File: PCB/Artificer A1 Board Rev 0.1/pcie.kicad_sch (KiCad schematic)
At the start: 1 part, among them U7 X3113WVS-36-9TV01

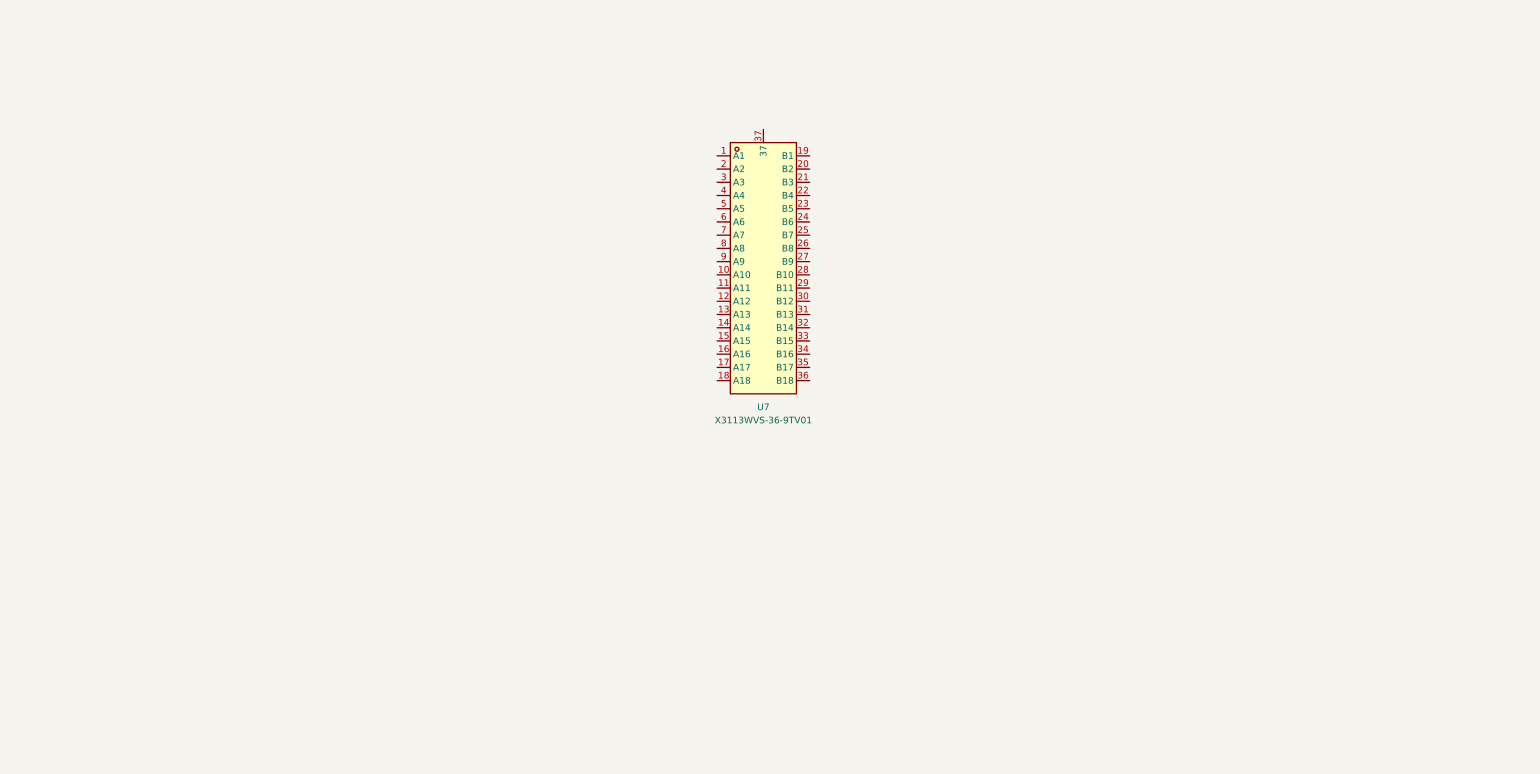
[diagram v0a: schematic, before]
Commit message: schematic update
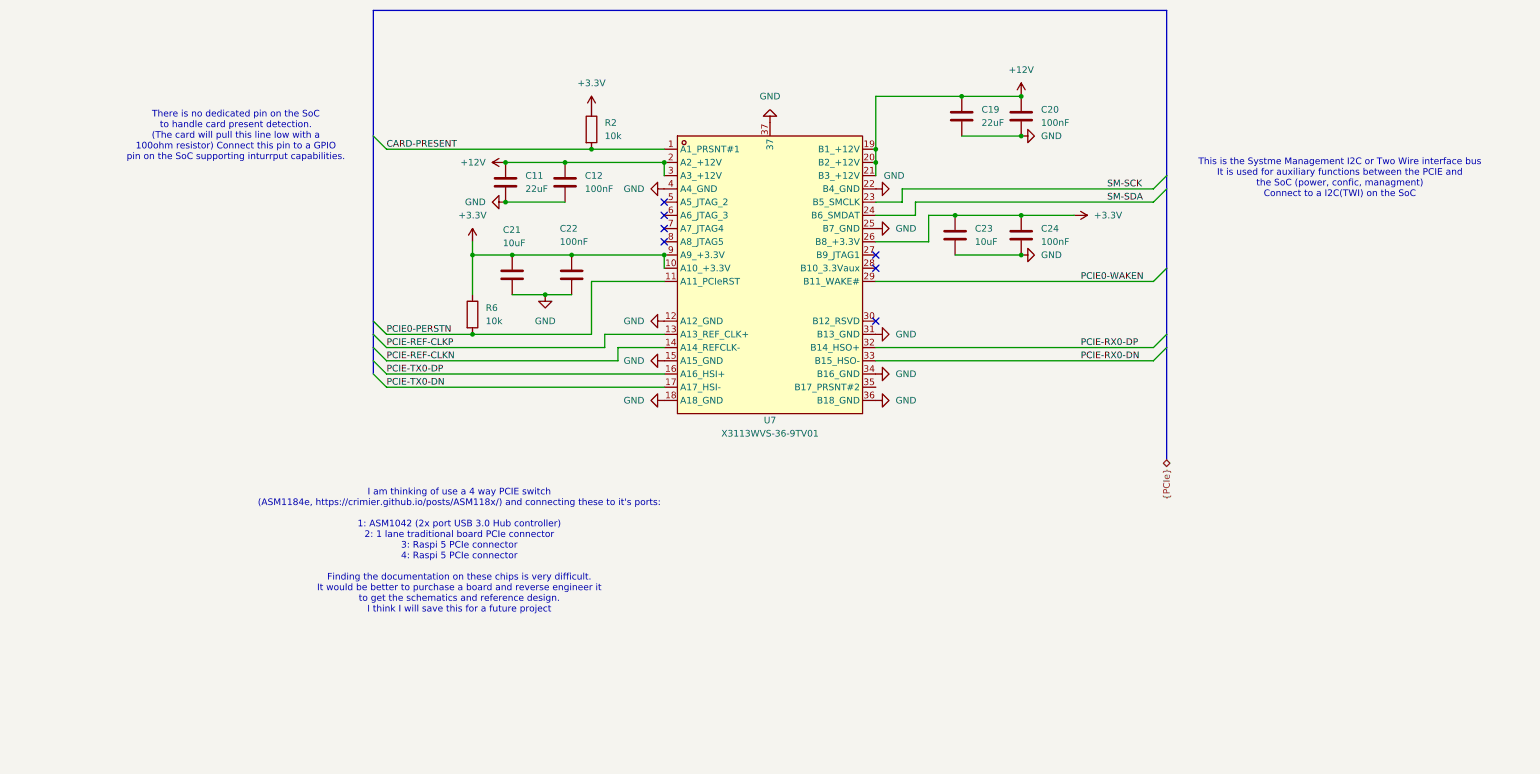
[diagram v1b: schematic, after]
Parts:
- added C11, C19: 22uF, symbol Device:C
- added C12, C20, C22, C24: 100nF, symbol Device:C
- added C21, C23: 10uF, symbol Device:C
- added R2, R6: 10k, symbol Device:R
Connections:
- net CARD-PRESENT: now reaches U7.1 (A1_PRSNT#1)
- net CARD-PRESENT: now also R2.2
- net +3.3V: now reaches U7.10 (A10_+3.3V)
- net +3.3V: now also U7.26 (B8_+3.3V), U7.9 (A9_+3.3V), C21.1, C22.1, C23.1, C24.1, R2.1, R6.1
- net PCIE0-PERSTN: now reaches U7.11 (A11_PCIeRST)
- net PCIE0-PERSTN: now also R6.2
- net GND: now reaches U7.12 (A12_GND)
- net GND: now also U7.15 (A15_GND), U7.18 (A18_GND), U7.22 (B4_GND), U7.25 (B7_GND), U7.31 (B13_GND), U7.34 (B16_GND), U7.36 (B18_GND), U7.37, U7.4 (A4_GND), C11.2, C12.2, C19.2, C20.2, C21.2, C22.2, C23.2, C24.2
- net PCIE-REF-CLKP : now reaches U7.13 (A13_REF_CLK+)
- net PCIE-REF-CLKN : now reaches U7.14 (A14_REFCLK-)
- net PCIE-TX0-DP: now reaches U7.16 (A16_HSI+)
- net PCIE-TX0-DN: now reaches U7.17 (A17_HSI-)
- net +12V: now reaches U7.19 (B1_+12V)
- net +12V: now also U7.2 (A2_+12V), U7.20 (B2_+12V), U7.21 (B3_+12V), U7.3 (A3_+12V), C11.1, C12.1, C19.1, C20.1
- net SM-SCK: now reaches U7.23 (B5_SMCLK)
- net SM-SDA: now reaches U7.24 (B6_SMDAT)
- net PCIE0-WAKEN : now reaches U7.29 (B11_WAKE#)
- net PCIE-RX0-DP: now reaches U7.32 (B14_HSO+)
- net PCIE-RX0-DN: now reaches U7.33 (B15_HSO-)
- no-connect marks 0 -> 7
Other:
- note added: "I am thinking of use a 4 way PCIE switch (ASM1184e, https://crimier.github.io/posts/ASM118x/) and connecting these to it's ports: 1: ASM1042 (2x port USB 3.0 Hub controller) 2: 1 lane traditional board PCIe connector 3: Raspi 5 PCIe connector 4: Raspi 5 PCIe connector Finding the documentation on these chips is very difficult. It would be better to purchase a board and reverse engineer it to get 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"
- note added: "There is no dedicated pin on the SoC to handle card present detection. (The card will pull this line low with a 100ohm resistor) Connect this pin to a GPIO pin on the SoC supporting inturrput capabilities."
- note added: "This is the Systme Management I2C or Two Wire interface bus It is used for auxiliary functions between the PCIE and the SoC (power, confic, managment) Connect to a I2C(TWI) on the SoC"
- moved on the sheet: U7

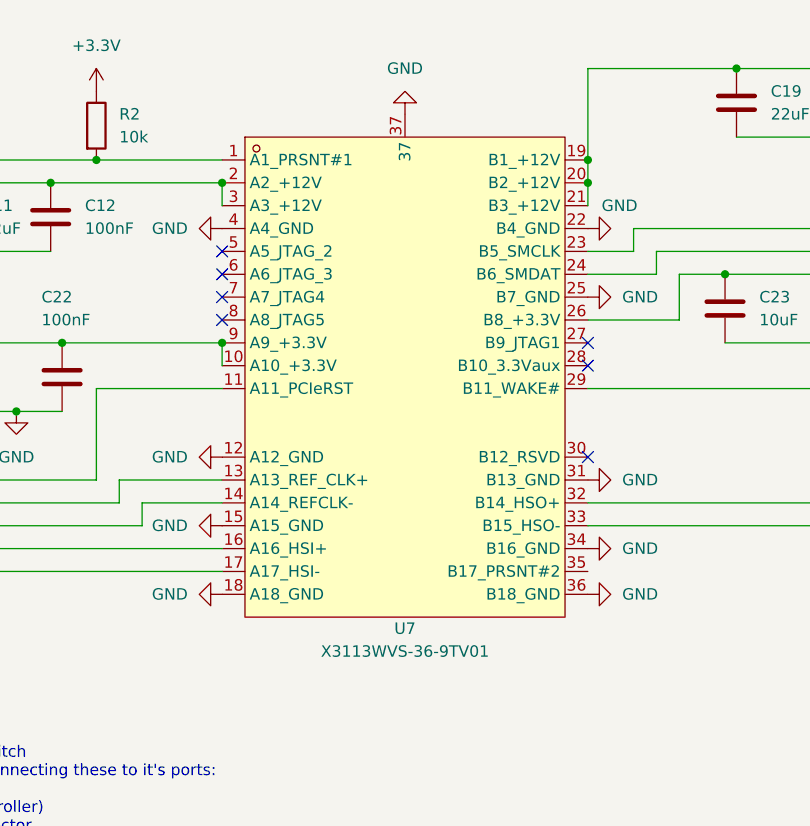
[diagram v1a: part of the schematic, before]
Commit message: localized libraries
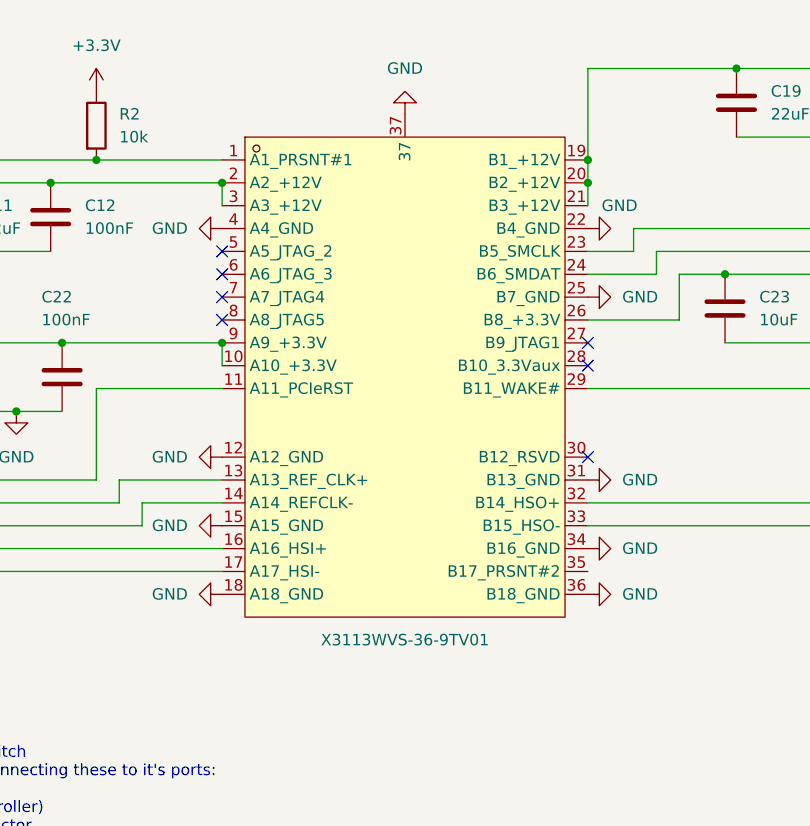
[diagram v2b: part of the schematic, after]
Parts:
- removed U7: X3113WVS-36-9TV01, easyeda2kicad:CONN-SMD_X3113WVS-36-9TV01, symbol easyeda2kicad:X3113WVS-36-9TV01
- added U7: X3113WVS-36-9TV01, easyeda:CONN-SMD_X3113WVS-36-9TV01, symbol easyeda:X3113WVS-36-9TV01
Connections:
- net +12V: now also U7.19 (B1_+12V), U7.2 (A2_+12V), U7.20 (B2_+12V), U7.21 (B3_+12V), U7.3 (A3_+12V)
- net +3.3V: now also U7.10 (A10_+3.3V), U7.26 (B8_+3.3V), U7.9 (A9_+3.3V)
- net CARD-PRESENT: now also U7.1 (A1_PRSNT#1)
- net GND: now also U7.12 (A12_GND), U7.15 (A15_GND), U7.18 (A18_GND), U7.22 (B4_GND), U7.25 (B7_GND), U7.31 (B13_GND), U7.34 (B16_GND), U7.36 (B18_GND), U7.37, U7.4 (A4_GND)
- net PCIE-REF-CLKN : now also U7.14 (A14_REFCLK-)
- net PCIE-REF-CLKP : now also U7.13 (A13_REF_CLK+)
- net PCIE-RX0-DN: now also U7.33 (B15_HSO-)
- net PCIE-RX0-DP: now also U7.32 (B14_HSO+)
- net PCIE-TX0-DN: now also U7.17 (A17_HSI-)
- net PCIE-TX0-DP: now also U7.16 (A16_HSI+)
- net PCIE0-PERSTN: now also U7.11 (A11_PCIeRST)
- net PCIE0-WAKEN : now also U7.29 (B11_WAKE#)
- net SM-SCK: now also U7.23 (B5_SMCLK)
- net SM-SDA: now also U7.24 (B6_SMDAT)

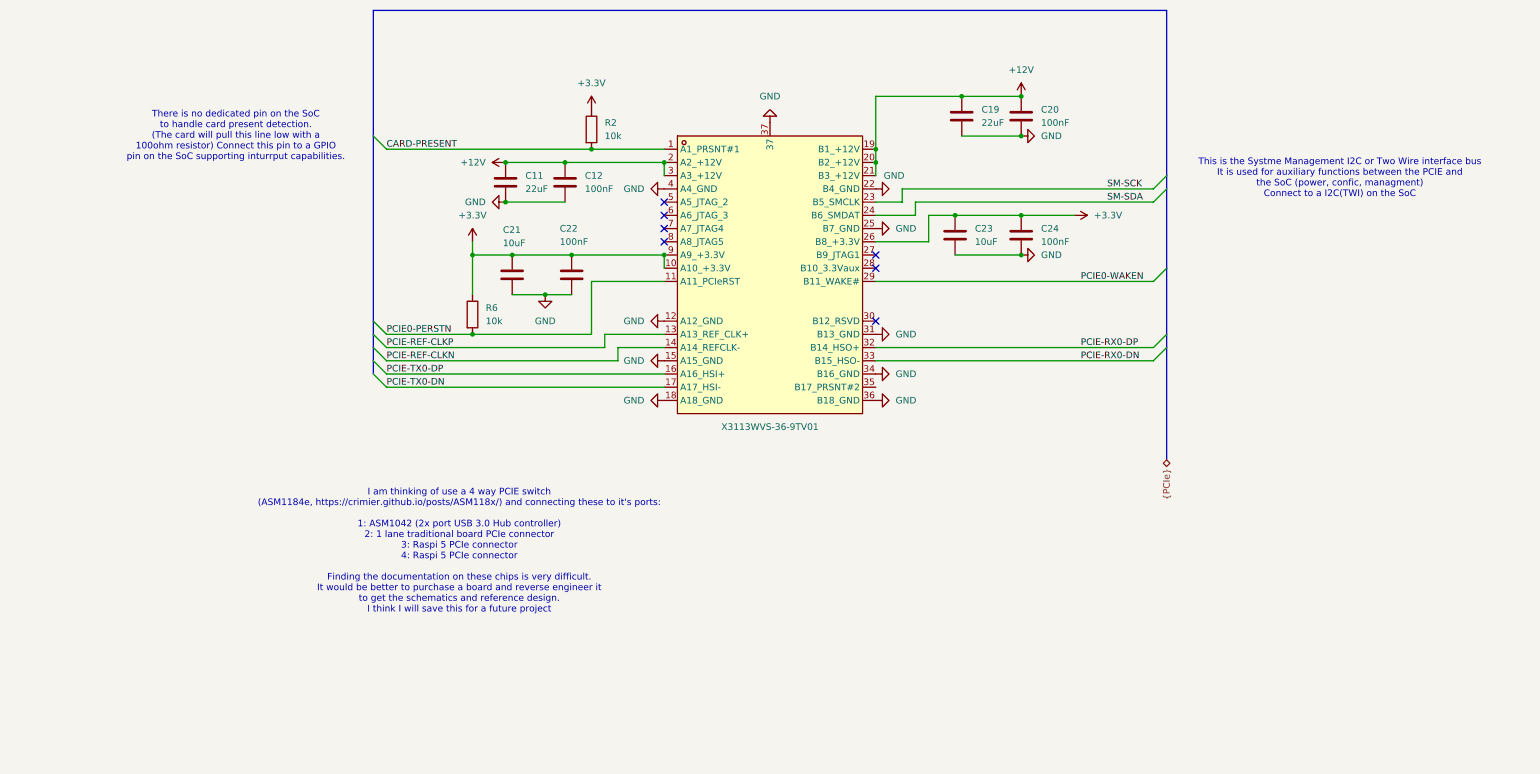
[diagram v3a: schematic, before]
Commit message: added: sd, wifi, audio, started power, fixed buses
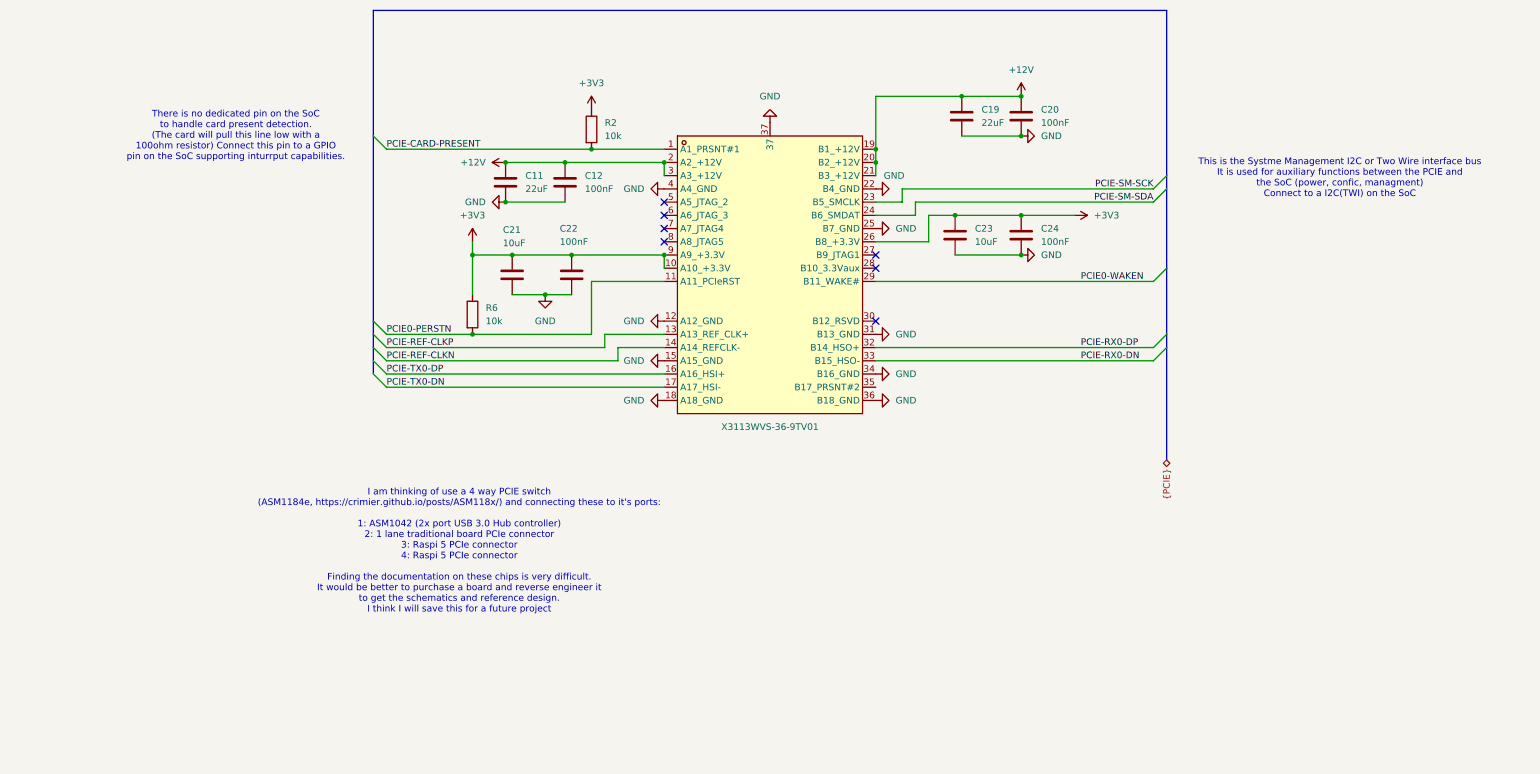
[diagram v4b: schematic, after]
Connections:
- net +3.3V renamed +3V3
- net CARD-PRESENT renamed PCIE-CARD-PRESENT
- net SM-SCK renamed PCIE-SM-SCK
- net SM-SDA renamed PCIE-SM-SDA

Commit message: added features
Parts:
- added R85: 0R, symbol Device:R_Small
- added U12: HD3SS3202IRSVR, easyeda:UQFN-16_L2.6-W1.8-P0.40-BL, symbol easyeda:HD3SS3202IRSVR
- added U17: HC-USB3.0-L168-WP, easyeda:USB-TH_USB3.0-A, symbol easyeda:HC-USB3.0-L168-WP
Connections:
- net at U7.28 (B10_3.3Vaux): now also R85.2
- net PCIE0-CLKREQN: now reaches U7.30 (B12_RSVD)
- net +3V3 renamed PCIE_3V3
- net PCIE_3V3: now also R85.1
- no-connect marks 7 -> 5
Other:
- moved on the sheet: C11, C12, C19, C20, C21, C22, C23, C24, R2, R6

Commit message: finished rough draft of power supply circuitry!
Yay! This one took a while
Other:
- moved on the sheet: U12, U17
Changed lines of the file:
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@@
 	(symbol
 		(lib_id "easyeda:HC-USB3.0-L168-WP")
-		(at 64.77 181.61 0)
+		(at 138.43 176.53 0)
 		(unit 1)
 		(exclude_from_sim no)
@@
 		(fields_autoplaced yes)
 		(property "Reference" "U17"
-			(at 63.5 163.83 0)
+			(at 137.16 158.75 0)
 			(effects
 				(font
@@
 		)
 		(property "Value" "HC-USB3.0-L168-WP"
-			(at 63.5 166.37 0)
+			(at 137.16 161.29 0)
 			(effects
 				(font
@@
 		)
 		(property "Footprint" "easyeda:USB-TH_USB3.0-A"
-			(at 64.77 199.39 0)
+			(at 138.43 194.31 0)
 			(effects
 				(font
@@
 		)
 		(property "Datasheet" ""
-			(at 64.77 181.61 0)
+			(at 138.43 176.53 0)
 			(effects
 				(font
@@
 		)
 		(property "Description" ""
-			(at 64.77 181.61 0)
+			(at 138.43 176.53 0)
 			(effects
 				(font
@@
 		)
 		(property "LCSC Part" "C7501850"
-			(at 64.77 201.93 0)
+			(at 138.43 196.85 0)
 			(effects
 				(font
@@
 	(symbol
 		(lib_id "easyeda:HD3SS3202IRSVR")
-		(at 97.79 180.34 0)
+		(at 66.04 176.53 0)
 		(unit 1)
 		(exclude_from_sim no)
@@
 		(fields_autoplaced yes)
 		(property "Reference" "U12"
-			(at 97.79 162.56 0)
+			(at 66.04 158.75 0)
 			(effects
 				(font
@@
 		)
 		(property "Value" "HD3SS3202IRSVR"
-			(at 97.79 165.1 0)
+			(at 66.04 161.29 0)
 			(effects
 				(font
@@
 		)
 		(property "Footprint" "easyeda:UQFN-16_L2.6-W1.8-P0.40-BL"
-			(at 97.79 195.58 0)
-			(effects
-				(font
-					(size 1.27 1.27)
-				)
-				(hide yes)
-			)
-		)
-		(property "Datasheet" ""
-			(at 97.79 180.34 0)
+			(at 66.04 191.77 0)
+			(effects
+				(font
+					(size 1.27 1.27)
+				)
+				(hide yes)
+			)
+		)
+		(property "Datasheet" "https://www.lcsc.com/datasheet/C2150836.pdf"
+			(at 66.04 176.53 0)
 			(effects
 				(font
@@
 		)
 		(property "Description" ""
-			(at 97.79 180.34 0)
+			(at 66.04 176.53 0)
 			(effects
 				(font
@@
 		)
 		(property "LCSC Part" "C2150836"
-			(at 97.79 198.12 0)
-			(effects
-				(font
+			(at 66.04 194.31 0)
+			(effects
+				(font
